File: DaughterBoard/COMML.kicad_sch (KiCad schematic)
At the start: 36 parts, among them J2 705510038, J3 705510038

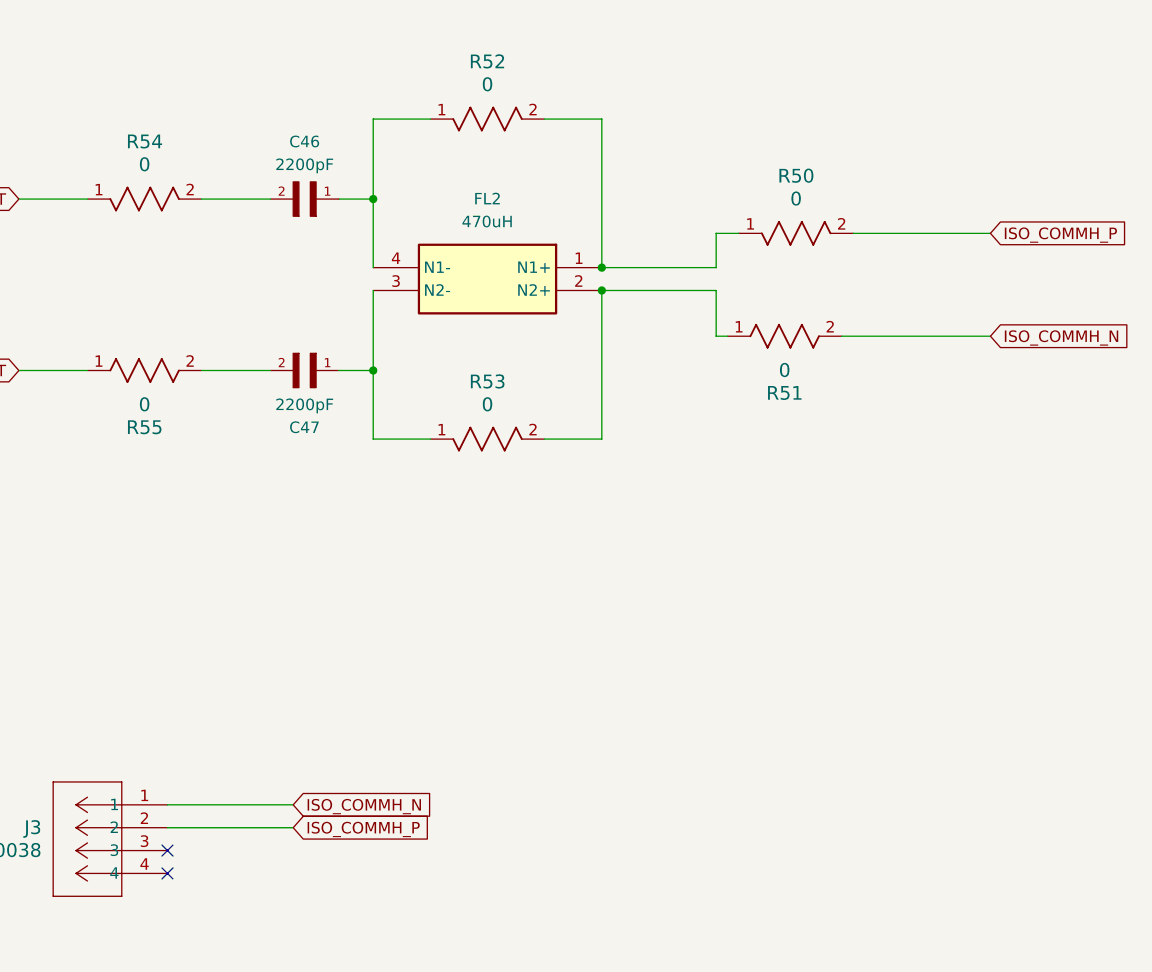
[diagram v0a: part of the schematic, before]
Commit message: Layout continued. Fixed Footprint and most 3d model
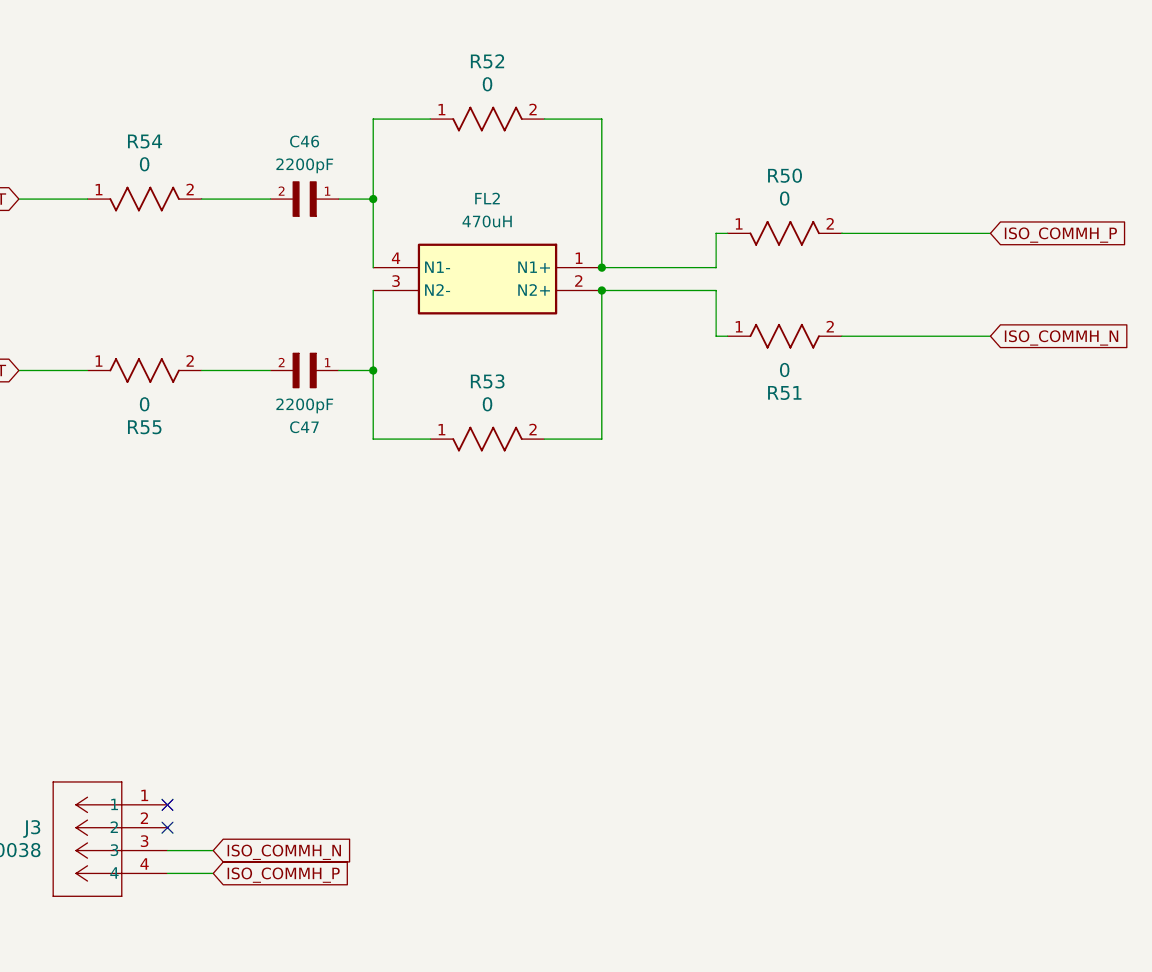
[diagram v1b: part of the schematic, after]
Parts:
- C40, C41: footprint CAP_CL10_SAM -> CL10B221JB8NNNC:CAP_CL10_SAM-L
- C43, C44, C46, C47: footprint 1206J2K00222KXR:CAPC3216X160N -> 1206J2K00222KXR (1):CAPC3216X160N
- FL1, FL2: footprint 744242471 -> KiCad:744242471
- J2, J3: footprint CONN_70551-xxxx_04_MOL -> 0705510038:CONN_70551-xxxx_04_MOL
- R34, R35: footprint RC0603N_VIS -> CRCW060351R0JNEA:RC0603N_VIS-L
- R36: footprint RC0603N_PAN -> ERJ-3EKF1001V:RC0603N_PAN-L
- R39, R40: footprint RC0603N_YAG -> RC0603JR-070RL:RC0603N_YAG-L
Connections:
- net ISO_COMMH_N: now also J3.3; no longer J3.1
- net ISO_COMMH_P: now also J3.4; no longer J3.2
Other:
- moved on the sheet: R50
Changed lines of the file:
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@@
 	)
 	(no_connect
-		(at 270.51 218.44)
+		(at 270.51 213.36)
 	)
 	(no_connect
-		(at 270.51 220.98)
+		(at 270.51 215.9)
 	)
 	(no_connect
@@
 	(wire
 		(pts
-			(xy 346.71 149.86) (xy 361.95 149.86)
+			(xy 345.44 149.86) (xy 361.95 149.86)
 		)
 		(stroke
@@
 	(wire
 		(pts
-			(xy 331.47 149.86) (xy 334.01 149.86)
+			(xy 331.47 149.86) (xy 332.74 149.86)
 		)
 		(stroke
@@
 	(wire
 		(pts
-			(xy 137.16 167.64) (xy 146.05 167.64)
+			(xy 270.51 220.98) (xy 275.59 220.98)
 		)
 		(stroke
@@
 	(wire
 		(pts
-			(xy 36.83 163.83) (xy 53.34 163.83)
+			(xy 137.16 167.64) (xy 146.05 167.64)
 		)
 		(stroke
@@
 	(wire
 		(pts
-			(xy 143.51 39.37) (xy 143.51 77.47)
+			(xy 36.83 163.83) (xy 53.34 163.83)
 		)
 		(stroke
@@
 	(wire
 		(pts
-			(xy 303.53 68.58) (xy 287.02 68.58)
+			(xy 143.51 39.37) (xy 143.51 77.47)
 		)
 		(stroke
@@
 	(wire
 		(pts
-			(xy 327.66 73.66) (xy 327.66 68.58)
+			(xy 303.53 68.58) (xy 287.02 68.58)
 		)
 		(stroke
@@
 	(wire
 		(pts
-			(xy 284.48 215.9) (xy 270.51 215.9)
+			(xy 327.66 73.66) (xy 327.66 68.58)
 		)
 		(stroke
@@
 	(wire
 		(pts
-			(xy 284.48 213.36) (xy 270.51 213.36)
+			(xy 80.01 139.7) (xy 86.36 139.7)
 		)
 		(stroke
@@
 	(wire
 		(pts
-			(xy 80.01 139.7) (xy 86.36 139.7)
+			(xy 322.58 39.37) (xy 322.58 73.66)
 		)
 		(stroke
@@
 	(wire
 		(pts
-			(xy 322.58 39.37) (xy 322.58 73.66)
+			(xy 270.51 218.44) (xy 275.59 218.44)
 		)
 		(stroke
@@
 	(global_label "ISO_COMMH_N"
 		(shape input)
-		(at 284.48 213.36 0)
+		(at 275.59 218.44 0)
 		(fields_autoplaced yes)
 		(effects
@@
 		)
 		(property "Intersheetrefs" "${INTERSHEET_REFS}"
-			(at 300.7095 213.36 0)
+			(at 291.8195 218.44 0)
 			(effects
 				(font
@@
 	(global_label "ISO_COMMH_P"
 		(shape input)
-		(at 284.48 215.9 0)
+		(at 275.59 220.98 0)
 		(fields_autoplaced yes)
 		(effects
@@
 		)
 		(property "Intersheetrefs" "${INTERSHEET_REFS}"
-			(at 300.649 215.9 0)
+			(at 291.759 220.98 0)
 			(effects
 				(font
@@
 			)
 		)
-		(property "Footprint" "RC0603N_VIS"
+		(property "Footprint" "CRCW060351R0JNEA:RC0603N_VIS-L"
 			(at 103.886 63.246 0)
 			(effects
@@
 			)
 		)
-		(property "Footprint" "1206J2K00222KXR:CAPC3216X160N"
+		(property "Footprint" "1206J2K00222KXR (1):CAPC3216X160N"
 			(at 111.76 167.64 0)
 			(effects
@@
 			)
 		)
-		(property "Footprint" "CONN_70551-xxxx_04_MOL"
+		(property "Footprint" "0705510038:CONN_70551-xxxx_04_MOL"
 			(at 270.51 213.36 0)
 			(effects
@@
 			)
 		)
-		(property "Footprint" "CONN_70551-xxxx_04_MOL"
+		(property "Footprint" "0705510038:CONN_70551-xxxx_04_MOL"
 			(at 138.43 219.71 0)
 			(effects
@@
 			)
 		)
-		(property "Footprint" "744242471"
+		(property "Footprint" "KiCad:744242471"
 			(at 101.6 251.13 0)
 			(effects
@@
 	(symbol
 		(lib_id "CRCW08050000Z0EAHP:CRCW08050000Z0EAHP")
-		(at 346.71 149.86 0)
+		(at 345.44 149.86 0)
 		(mirror y)
 		(unit 1)
@@
 		(fields_autoplaced yes)
 		(property "Reference" "R50"
-			(at 340.36 143.51 0)
+			(at 339.09 143.51 0)
 			(effects
 				(font
@@
 		)
 		(property "Value" "0"
-			(at 340.36 146.05 0)
+			(at 339.09 146.05 0)
 			(effects
 				(font
@@
 		)
 		(property "Footprint" "RES_CRCW_0805_VIS"
-			(at 346.71 157.226 0)
+			(at 345.44 157.226 0)
 			(effects
 				(font
@@
 		)
 		(property "Datasheet" "CRCW08050000Z0EAHP"
-			(at 346.71 157.226 0)
+			(at 345.44 157.226 0)
 			(effects
 				(font
@@
 		)
 		(property "Description" ""
-			(at 346.71 149.86 0)
+			(at 345.44 149.86 0)
 			(effects
 				(font
@@
 		)
 		(property "Manufacturer Part Number" "CRCW08050000Z0EAHP"
-			(at 346.71 149.86 0)
+			(at 345.44 149.86 0)
 			(effects
 				(font
@@
 			)
 		)
-		(property "Footprint" "1206J2K00222KXR:CAPC3216X160N"
+		(property "Footprint" "1206J2K00222KXR (1):CAPC3216X160N"
 			(at 287.02 146.05 0)
 			(effects
@@
 			)
 		)
-		(property "Footprint" "RC0603N_VIS"
+		(property "Footprint" "CRCW060351R0JNEA:RC0603N_VIS-L"
 			(at 100.838 28.956 0)
 			(effects
@@
 			)
 		)
-		(property "Footprint" "744242471"
+		(property "Footprint" "KiCad:744242471"
 			(at 297.18 248.59 0)
 			(effects
@@
 			)
 		)
-		(property "Footprint" "CAP_CL10_SAM"
+		(property "Footprint" "CL10B221JB8NNNC:CAP_CL10_SAM-L"
 			(at 139.954 85.598 0)
 			(effects
@@
 			)
 		)
-		(property "Footprint" "RC0603N_PAN"
+		(property "Footprint" "ERJ-3EKF1001V:RC0603N_PAN-L"
 			(at 153.162 46.228 0)
 			(effects
@@
 			)
 		)
-		(property "Footprint" "1206J2K00222KXR:CAPC3216X160N"
+		(property "Footprint" "1206J2K00222KXR (1):CAPC3216X160N"
 			(at 111.76 148.59 0)
 			(effects
@@
 			)
 		)
-		(property "Footprint" "1206J2K00222KXR:CAPC3216X160N"
+		(property "Footprint" "1206J2K00222KXR (1):CAPC3216X160N"
 			(at 287.02 165.1 0)
 			(effects
@@
 			)
 		)
-		(property "Footprint" "RC0603N_YAG"
+		(property "Footprint" "RC0603JR-070RL:RC0603N_YAG-L"
 			(at 344.17 41.91 0)
 			(effects
@@
 			)
 		)
-		(property "Footprint" "RC0603N_YAG"
+		(property "Footprint" "RC0603JR-070RL:RC0603N_YAG-L"
 			(at 346.964 57.404 0)
 			(effects
@@
 			)
 		)
-		(property "Footprint" "CAP_CL10_SAM"
+		(property "Footprint" "CL10B221JB8NNNC:CAP_CL10_SAM-L"
 			(at 139.192 83.82 0)
 			(effects

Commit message: tracing left
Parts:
- C42, C45: footprint CAP_CL10_SAM -> CL10B221JB8NNNC:CAP_CL10_SAM-L
- R34, R35: value 51 -> 51
- R37, R38: value 0 -> 0; footprint RC0603N_YAG -> RC0603JR-070RL:RC0603N_YAG-L
- R39, R40: value 0 -> 0
- R41, R42: value 51 -> 51; footprint RC0603N_VIS -> CRCW060351R0JNEA:RC0603N_VIS-L
- R43, R44, R45, R46, R47, R48, R50, R51, R52, R53, R54, R55: value 0 -> 0; footprint RES_CRCW_0805_VIS -> CRCW08050000Z0EAHP:RES_CRCW_0805_VIS-L
- R49: value 1K -> 1k; footprint RC0603N_PAN -> ERJ-3EKF1001V:RC0603N_PAN-L

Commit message: Connectors
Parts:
- removed J2, J3: 705510038, 0705510038:CONN_70551-xxxx_04_MOL, symbol 0705510038:705510038
- added J1, J5: 430450200, 0430450200:CON_430450200_MOL, symbol 0430450200:430450200
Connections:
- net ISO_COMMH_N: now also J5.2
- net ISO_COMMH_P: now also J5.1
- net ISO_COMML_N: now also J1.1
- net ISO_COMML_P: now also J1.2
- no-connect marks 4 -> 0
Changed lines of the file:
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@@
 		(color 0 0 0 0)
 	)
-	(no_connect
-		(at 138.43 227.33)
-	)
-	(no_connect
-		(at 270.51 213.36)
-	)
-	(no_connect
-		(at 270.51 215.9)
-	)
-	(no_connect
-		(at 138.43 224.79)
-	)
 	(wire
 		(pts
@@
 	(wire
 		(pts
-			(xy 124.46 222.25) (xy 138.43 222.25)
-		)
-		(stroke
-			(width 0)
-			(type default)
-		)
-	)
-	(wire
-		(pts
 			(xy 293.37 137.16) (xy 293.37 146.05)
 		)
@@
 	(wire
 		(pts
-			(xy 124.46 219.71) (xy 138.43 219.71)
-		)
-		(stroke
-			(width 0)
-			(type default)
-		)
-	)
-	(wire
-		(pts
 			(xy 109.22 167.64) (xy 105.41 167.64)
 		)
@@
 	(wire
 		(pts
-			(xy 270.51 220.98) (xy 275.59 220.98)
-		)
-		(stroke
-			(width 0)
-			(type default)
-		)
-	)
-	(wire
-		(pts
 			(xy 137.16 167.64) (xy 146.05 167.64)
 		)
@@
 	(wire
 		(pts
-			(xy 270.51 218.44) (xy 275.59 218.44)
-		)
-		(stroke
-			(width 0)
-			(type default)
-		)
-	)
-	(wire
-		(pts
 			(xy 116.84 148.59) (xy 124.46 148.59)
 		)
@@
 	(global_label "ISO_COMMH_N"
 		(shape input)
-		(at 275.59 218.44 0)
+		(at 270.51 234.95 0)
 		(fields_autoplaced yes)
 		(effects
@@
 		)
 		(property "Intersheetrefs" "${INTERSHEET_REFS}"
-			(at 291.8195 218.44 0)
+			(at 286.7395 234.95 0)
 			(effects
 				(font
@@
 	(global_label "ISO_COMML_N"
 		(shape input)
-		(at 124.46 219.71 180)
+		(at 138.43 234.95 180)
 		(fields_autoplaced yes)
 		(effects
@@
 		)
 		(property "Intersheetrefs" "${INTERSHEET_REFS}"
-			(at 108.5329 219.71 0)
+			(at 122.5029 234.95 0)
 			(effects
 				(font
@@
 	(global_label "ISO_COMML_P"
 		(shape input)
-		(at 124.46 222.25 180)
+		(at 138.43 237.49 180)
 		(fields_autoplaced yes)
 		(effects
@@
 		)
 		(property "Intersheetrefs" "${INTERSHEET_REFS}"
-			(at 108.5934 222.25 0)
+			(at 122.5634 237.49 0)
 			(effects
 				(font
@@
 	(global_label "ISO_COMMH_P"
 		(shape input)
-		(at 275.59 220.98 0)
+		(at 270.51 237.49 0)
 		(fields_autoplaced yes)
 		(effects
@@
 		)
 		(property "Intersheetrefs" "${INTERSHEET_REFS}"
-			(at 291.759 220.98 0)
+			(at 286.679 237.49 0)
 			(effects
 				(font
@@
 	)
 	(symbol
-		(lib_id "0705510038:705510038")
-		(at 270.51 213.36 0)
-		(mirror y)
-		(unit 1)
-		(exclude_from_sim no)
-		(in_bom yes)
-		(on_board yes)
-		(dnp no)
-		(fields_autoplaced yes)
-		(property "Reference" "J3"
-			(at 256.54 215.8999 0)
-			(effects
-				(font
-					(size 1.524 1.524)
-				)
-				(justify left)
-			)
-		)
-		(property "Value" "705510038"
-			(at 256.54 218.4399 0)
-			(effects
-				(font
-					(size 1.524 1.524)
-				)
-				(justify left)
-			)
-		)
-		(property "Footprint" "0705510038:CONN_70551-xxxx_04_MOL"
-			(at 270.51 213.36 0)
-			(effects
-				(font
-					(size 1.27 1.27)
-					(italic yes)
-				)
-				(hide yes)
-			)
-		)
-		(property "Datasheet" "https://tools.molex.com/pdm_docs/ps/PS-70400.pdf"
-			(at 270.51 213.36 0)
-			(effects
-				(font
-					(size 1.27 1.27)
-					(italic yes)
-				)
-				(hide yes)
-			)
-		)
-		(property "Description" ""
-			(at 270.51 213.36 0)
-			(effects
-				(font
-					(size 1.27 1.27)
-				)
-				(hide yes)
-			)
-		)
-		(property "Manufacturer Part Number" "0705510038"
-			(at 270.51 213.36 0)
-			(effects
-				(font
-					(size 1.27 1.27)
-				)
-				(hide yes)
-			)
-		)
-		(pin "4"
-		)
-		(pin "2"
-		)
-		(pin "1"
-		)
-		(pin "3"
-		)
-		(instances
-			(project "Project63_BMS_DaughterBoard"
-				(path "/325b096d-8e4c-4cdc-b4c5-634ea5e73c60/8d4a348c-1e09-4dff-8656-797547bf484e"
-					(reference "J3")
-					(unit 1)
-				)
-			)
-		)
-	)
-	(symbol
 		(lib_name "CRCW08050000Z0EAHP_1")
 		(lib_id "CRCW08050000Z0EAHP:CRCW08050000Z0EAHP")
@@
 	)
 	(symbol
-		(lib_id "0705510038:705510038")
-		(at 138.43 219.71 0)
-		(unit 1)
-		(exclude_from_sim no)
-		(in_bom yes)
-		(on_board yes)
-		(dnp no)
-		(fields_autoplaced yes)
-		(property "Reference" "J2"
-			(at 152.4 222.2499 0)
-			(effects
-				(font
-					(size 1.524 1.524)
-				)
-				(justify left)
-			)
-		)
-		(property "Value" "705510038"
-			(at 152.4 224.7899 0)
-			(effects
-				(font
-					(size 1.524 1.524)
-				)
-				(justify left)
-			)
-		)
-		(property "Footprint" "0705510038:CONN_70551-xxxx_04_MOL"
-			(at 138.43 219.71 0)
-			(effects
-				(font
-					(size 1.27 1.27)
-					(italic yes)
-				)
-				(hide yes)
-			)
-		)
-		(property "Datasheet" "https://tools.molex.com/pdm_docs/ps/PS-70400.pdf"
-			(at 138.43 219.71 0)
-			(effects
-				(font
-					(size 1.27 1.27)
-					(italic yes)
-				)
-				(hide yes)
-			)
-		)
-		(property "Description" ""
-			(at 138.43 219.71 0)
-			(effects
-				(font
-					(size 1.27 1.27)
-				)
-				(hide yes)
-			)
-		)
-		(property "Manufacturer Part Number" "0705510038"
-			(at 138.43 219.71 0)
-			(effects
-				(font
-					(size 1.27 1.27)
-				)
-				(hide yes)
-			)
-		)
-		(pin "4"
-		)
-		(pin "2"
-		)
-		(pin "1"
-		)
-		(pin "3"
-		)
-		(instances
-			(project "Project63_BMS_DaughterBoard"
-				(path "/325b096d-8e4c-4cdc-b4c5-634ea5e73c60/8d4a348c-1e09-4dff-8656-797547bf484e"
-					(reference "J2")
-					(unit 1)
-				)
-			)
-		)
-	)
-	(symbol
 		(lib_name "CRCW08050000Z0EAHP_1")
 		(lib_id "CRCW08050000Z0EAHP:CRCW08050000Z0EAHP")
@@
 	)
 	(symbol
+		(lib_id "0430450200:430450200")
+		(at 138.43 234.95 0)
+		(unit 1)
+		(exclude_from_sim no)
+		(in_bom yes)
+		(on_board yes)
+		(dnp no)
+		(fields_autoplaced yes)
+		(property "Reference" "J1"
+			(at 152.4 234.9499 0)
+			(effects
+				(font
+					(size 1.524 1.524)
+				)
+				(justify left)
+			)
+		)
+		(property "Value" "430450200"
+			(at 152.4 237.4899 0)
+			(effects
+				(font
+					(size 1.524 1.524)
+				)
+				(justify left)
+			)
+		)
+		(property "Footprint" "0430450200:CON_430450200_MOL"
+			(at 138.43 234.95 0)
+			(effects
+				(font
+					(size 1.27 1.27)
+					(italic yes)
+				)
+				(hide yes)
+			)
+		)
+		(property "Datasheet" "430450200"
+			(at 138.43 234.95 0)
+			(effects
+				(font
+					(size 1.27 1.27)
+					(italic yes)
+				)
+				(hide yes)
+			)
+		)
+		(property "Description" ""
+			(at 138.43 234.95 0)
+			(effects
+				(font
+					(size 1.27 1.27)
+				)
+				(hide yes)
+			)
+		)
+		(pin "2"
+		)
+		(pin "1"
+		)
+		(instances
+			(project "Project63_BMS_DaughterBoard"
+				(path "/325b096d-8e4c-4cdc-b4c5-634ea5e73c60/8d4a348c-1e09-4dff-8656-797547bf484e"
+					(reference "J1")
+					(unit 1)
+				)
+			)
+		)
+	)
+	(symbol
 		(lib_name "CRCW08050000Z0EAHP_1")
 		(lib_id "CRCW08050000Z0EAHP:CRCW08050000Z0EAHP")
@@
 					(unit 1)
 				)
+			)
+		)
+	)
+	(symbol
+		(lib_id "0430450200:430450200")
+		(at 270.51 237.49 180)
+		(unit 1)
+		(exclude_from_sim no)
+		(in_bom yes)
+		(on_board yes)
+		(dnp no)
+		(fields_autoplaced yes)
+		(property "Reference" "J5"
+			(at 261.62 227.33 0)
+			(effects
+				(font
+					(size 1.524 1.524)
+				)
+			)
+		)
+		(property "Value" "430450200"
+			(at 261.62 229.87 0)
+			(effects
+				(font
+					(size 1.524 1.524)
+				)
+			)
+		)
+		(property "Footprint" "0430450200:CON_430450200_MOL"
+			(at 270.51 237.49 0)
+			(effects
+				(font
+					(size 1.27 1.27)
+					(italic yes)
+				)
+				(hide yes)
+			)
+		)
+		(property "Datasheet" "430450200"
+			(at 270.51 237.49 0)
+			(effects
+				(font
+					(size 1.27 1.27)
+					(italic yes)
+				)
+				(hide yes)
+			)
+		)
+		(property "Description" ""
+			(at 270.51 237.49 0)
+			(effects
+				(font
+					(size 1.27 1.27)
+				)
+				(hide yes)
+			)
+		)
+		(pin "2"
+		)
+		(pin "1"
+		)
+		(instances
+			(project "Project63_BMS_DaughterBoard"
+				(path "/325b096d-8e4c-4cdc-b4c5-634ea5e73c60/8d4a348c-1e09-4dff-8656-797547bf484e"
+					(reference "J5")
+					(unit 1)
+				)

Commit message: done
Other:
- moved on the sheet: J5
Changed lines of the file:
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@@
 	(global_label "ISO_COMMH_N"
 		(shape input)
-		(at 270.51 234.95 0)
+		(at 257.81 238.76 180)
 		(fields_autoplaced yes)
 		(effects
@@
 				(size 1.27 1.27)
 			)
-			(justify left)
+			(justify right)
 		)
 		(property "Intersheetrefs" "${INTERSHEET_REFS}"
-			(at 286.7395 234.95 0)
+			(at 241.5805 238.76 0)
 			(effects
 				(font
 					(size 1.27 1.27)
 				)
-				(justify left)
+				(justify right)
 				(hide yes)
 			)
@@
 	(global_label "ISO_COMMH_P"
 		(shape input)
-		(at 270.51 237.49 0)
+		(at 257.81 236.22 180)
 		(fields_autoplaced yes)
 		(effects
@@
 				(size 1.27 1.27)
 			)
-			(justify left)
+			(justify right)
 		)
 		(property "Intersheetrefs" "${INTERSHEET_REFS}"
-			(at 286.679 237.49 0)
+			(at 241.641 236.22 0)
 			(effects
 				(font
 					(size 1.27 1.27)
 				)
-				(justify left)
+				(justify right)
 				(hide yes)
 			)
@@
 	(symbol
 		(lib_id "0430450200:430450200")
-		(at 270.51 237.49 180)
+		(at 257.81 236.22 0)
 		(unit 1)
 		(exclude_from_sim no)
@@
 		(fields_autoplaced yes)
 		(property "Reference" "J5"
-			(at 261.62 227.33 0)
+			(at 266.7 246.38 0)
 			(effects
 				(font
@@
 		)
 		(property "Value" "430450200"
-			(at 261.62 229.87 0)
+			(at 266.7 243.84 0)
 			(effects
 				(font
@@
 		)
 		(property "Footprint" "0430450200:CON_430450200_MOL"
-			(at 270.51 237.49 0)
+			(at 257.81 236.22 0)
 			(effects
 				(font
@@
 		)
 		(property "Datasheet" "430450200"
-			(at 270.51 237.49 0)
+			(at 257.81 236.22 0)
 			(effects
 				(font
@@
 		)
 		(property "Description" ""
-			(at 270.51 237.49 0)
+			(at 257.81 236.22 0)
 			(effects
 				(font

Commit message: Routing Update 3
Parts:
- R34, R35, R41, R42: value 51 -> 51
- R37, R38, R39, R40, R43, R44, R45, R46, R47, R48, R50, R51, R52, R53, R54, R55: value 0 -> 0
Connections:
- net COMHN: now also C45.2; no longer C42.2
- net COMHP: now also C42.2; no longer C45.2
- net ISO_COMMH_N: now also R50.2; no longer R51.2
- net ISO_COMMH_P: now also R51.2; no longer R50.2
- net at R35.2, R37.2: now also D2.1; no longer D2.2
- net at R34.2, R38.2: now also D2.2; no longer D2.1
- net COMMH_N_OPT renamed COMMH_N_OPT-
- net COMMH_N_OPT-: now also R54.1; no longer R55.1
- net COMMH_P_OPT renamed COMMH_P_OPT+
- net COMMH_P_OPT+: now also R55.1; no longer R54.1
- net COMML_N_OPT renamed COMML_N_OPT-
- net COMML_P_OPT renamed COMML_P_OPT+
- net GND renamed GND_CVSS
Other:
- moved on the sheet: J5
